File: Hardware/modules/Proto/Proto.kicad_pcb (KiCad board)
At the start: 2 copper layers, 83.3 x 68.2 mm, 529 parts, among them J1 Bus_PCI_6502, J2 Bus_PCI_6502

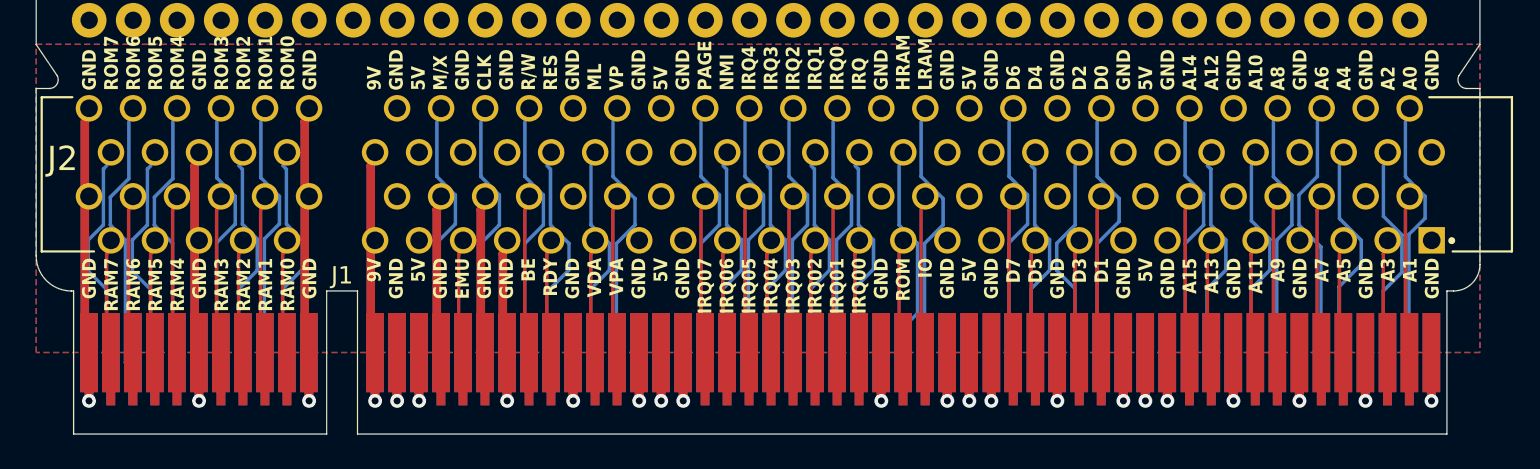
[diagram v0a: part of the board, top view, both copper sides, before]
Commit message: Hardware Review Pt. 1 fix Address Decoding for Strobe Generators add bulk capacitance to every board fix wiring of Prototyping Board
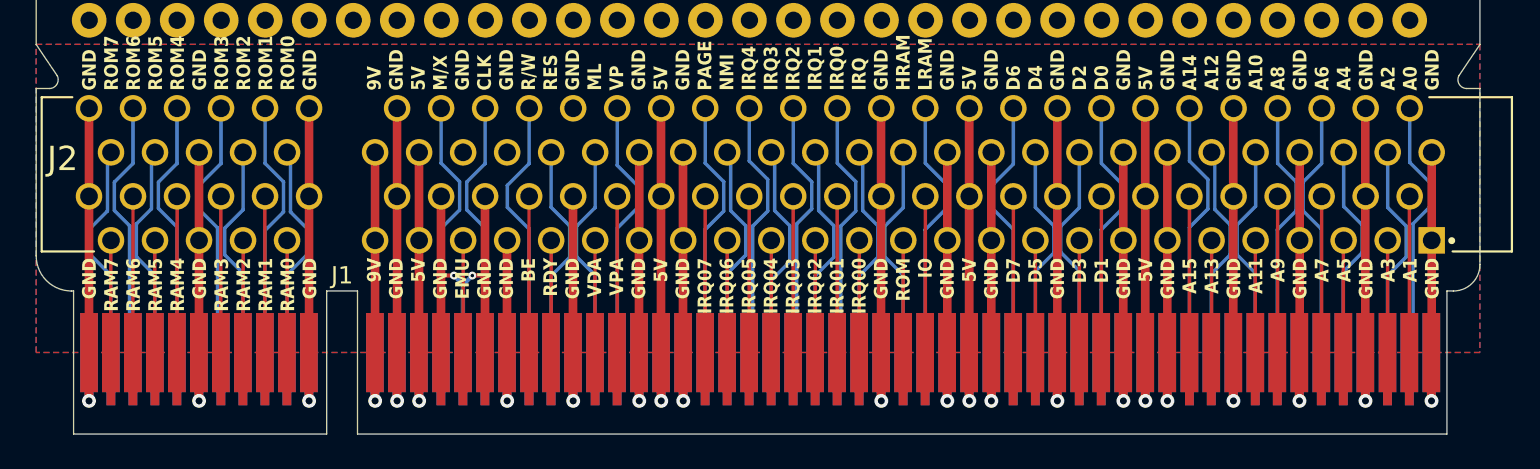
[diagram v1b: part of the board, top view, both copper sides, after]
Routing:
- net GND: track 64.3 -> 243.2 mm, vias 18 -> 20
- net +5V: track 0.00 -> 53.9 mm
